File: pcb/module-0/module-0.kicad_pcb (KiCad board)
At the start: 2 copper layers, 76 x 176 mm, 28 parts, among them J1 Conn_01x06, J2 Conn_01x06, SW1 SW_Push, SW2 SW_Push, SW3 SW_Push, SW4 SW_Push, SW5 RotaryEncoder_Switch_MP, U1 ESP32 S3 L, U2 MCP23S17_SO, U3 74AHC541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

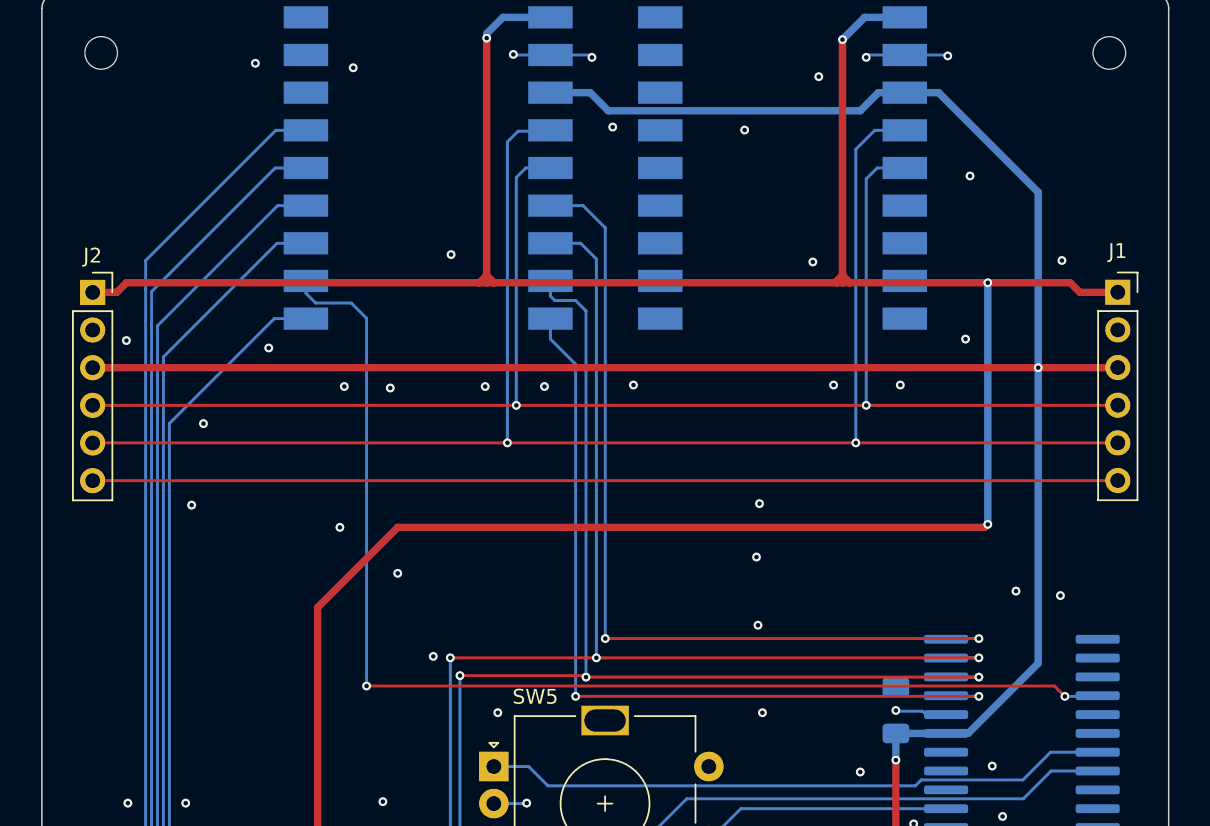
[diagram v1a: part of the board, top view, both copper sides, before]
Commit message: 3V net should not be shared across the bus
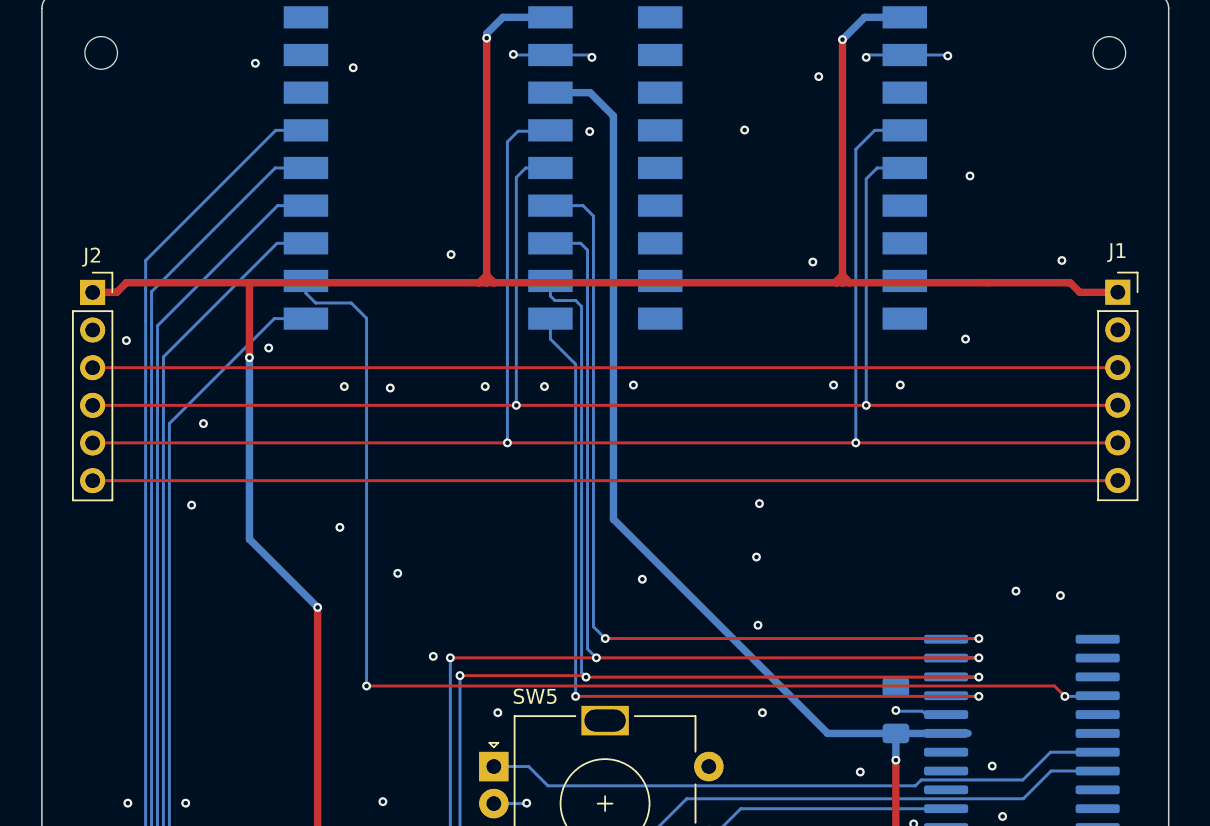
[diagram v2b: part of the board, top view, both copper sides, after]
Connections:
- C1 pad 1: 3V3 -> /3V3
- J1 pad 3: 3V3 -> Net-(J1-Pin_3)
- J2 pad 3: 3V3 -> Net-(J1-Pin_3)
- LCD1 pad 2: 3V3 -> /3V3
- U1 pad 3: 3V3 -> /3V3
- U2 pad 9: 3V3 -> /3V3
- U4 pad 3: 3V3 -> unconnected-(U4-V3V-Pad3)
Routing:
- net 3V3: track 225.7 -> 0.00 mm, vias 2 -> 0
- net /3V3: track 0.00 -> 138.6 mm, vias 0 -> 1
- net Net-(J1-Pin_3): track 0.00 -> 69.1 mm
- net 5V: track 389.3 -> 349.3 mm
- net GND: vias 79 -> 80
